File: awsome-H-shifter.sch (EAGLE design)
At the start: 8 parts

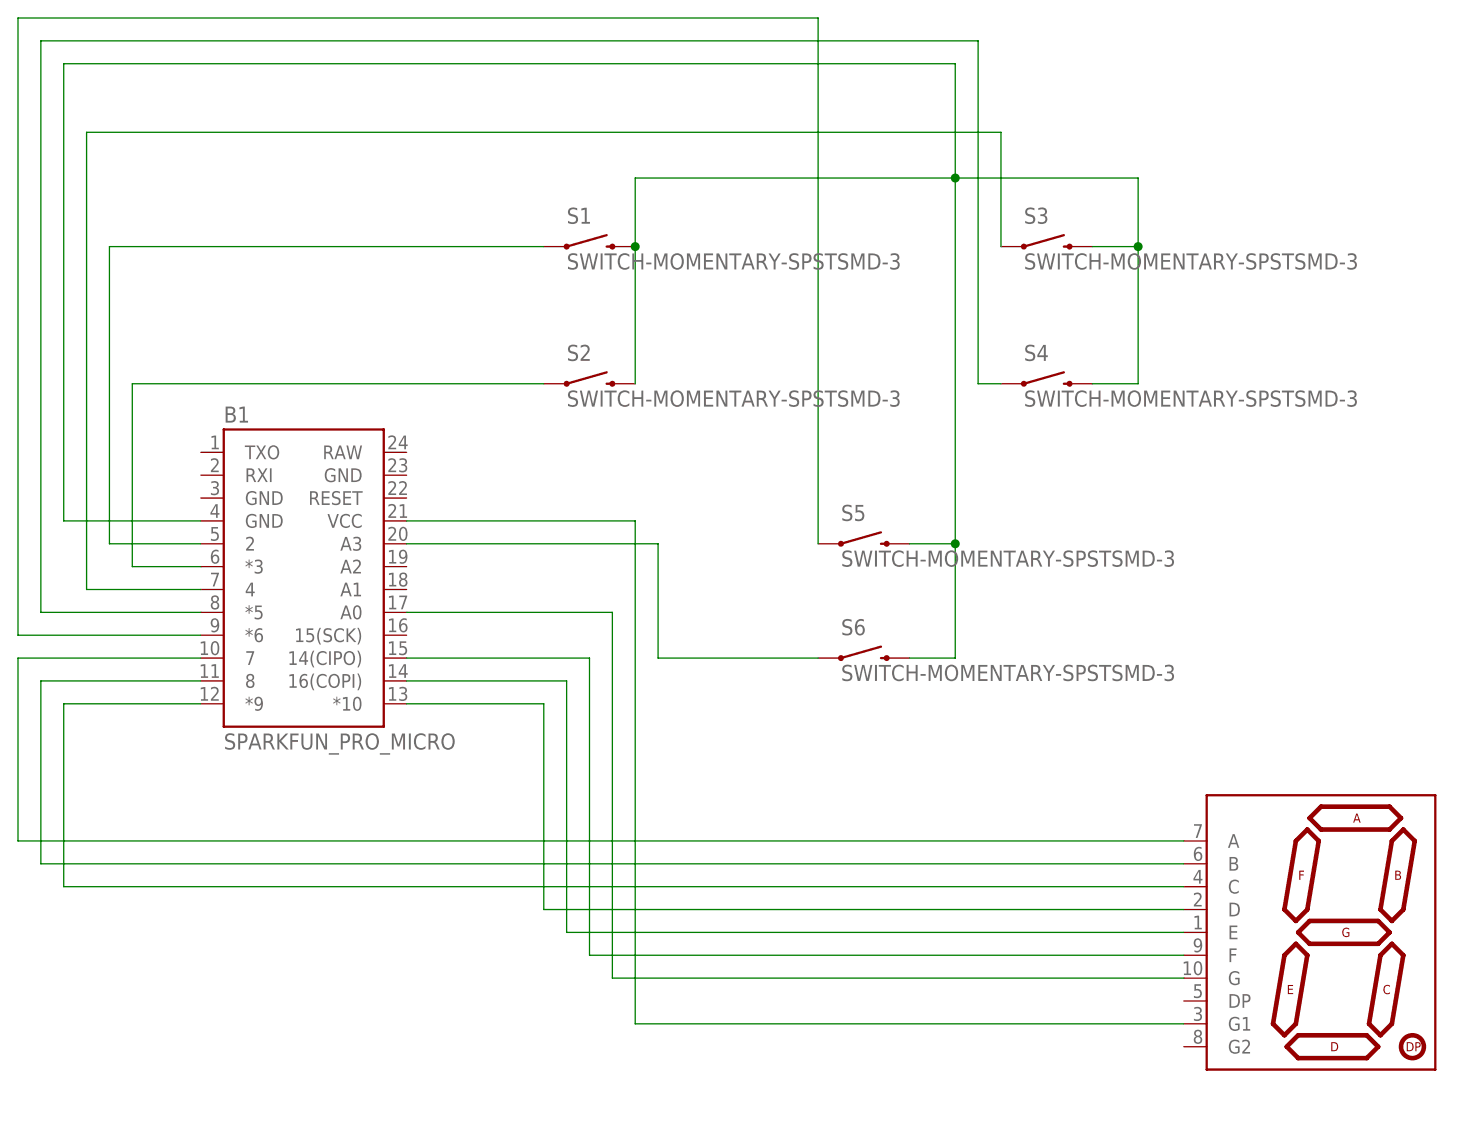
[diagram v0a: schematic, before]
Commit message: Add resistor library and R1 part to schematic
Integrated the 'Resistor' library with multiple resistor packages and symbols, and added a new resistor part R1 (300 Ω, 0402 package) to the schematic.
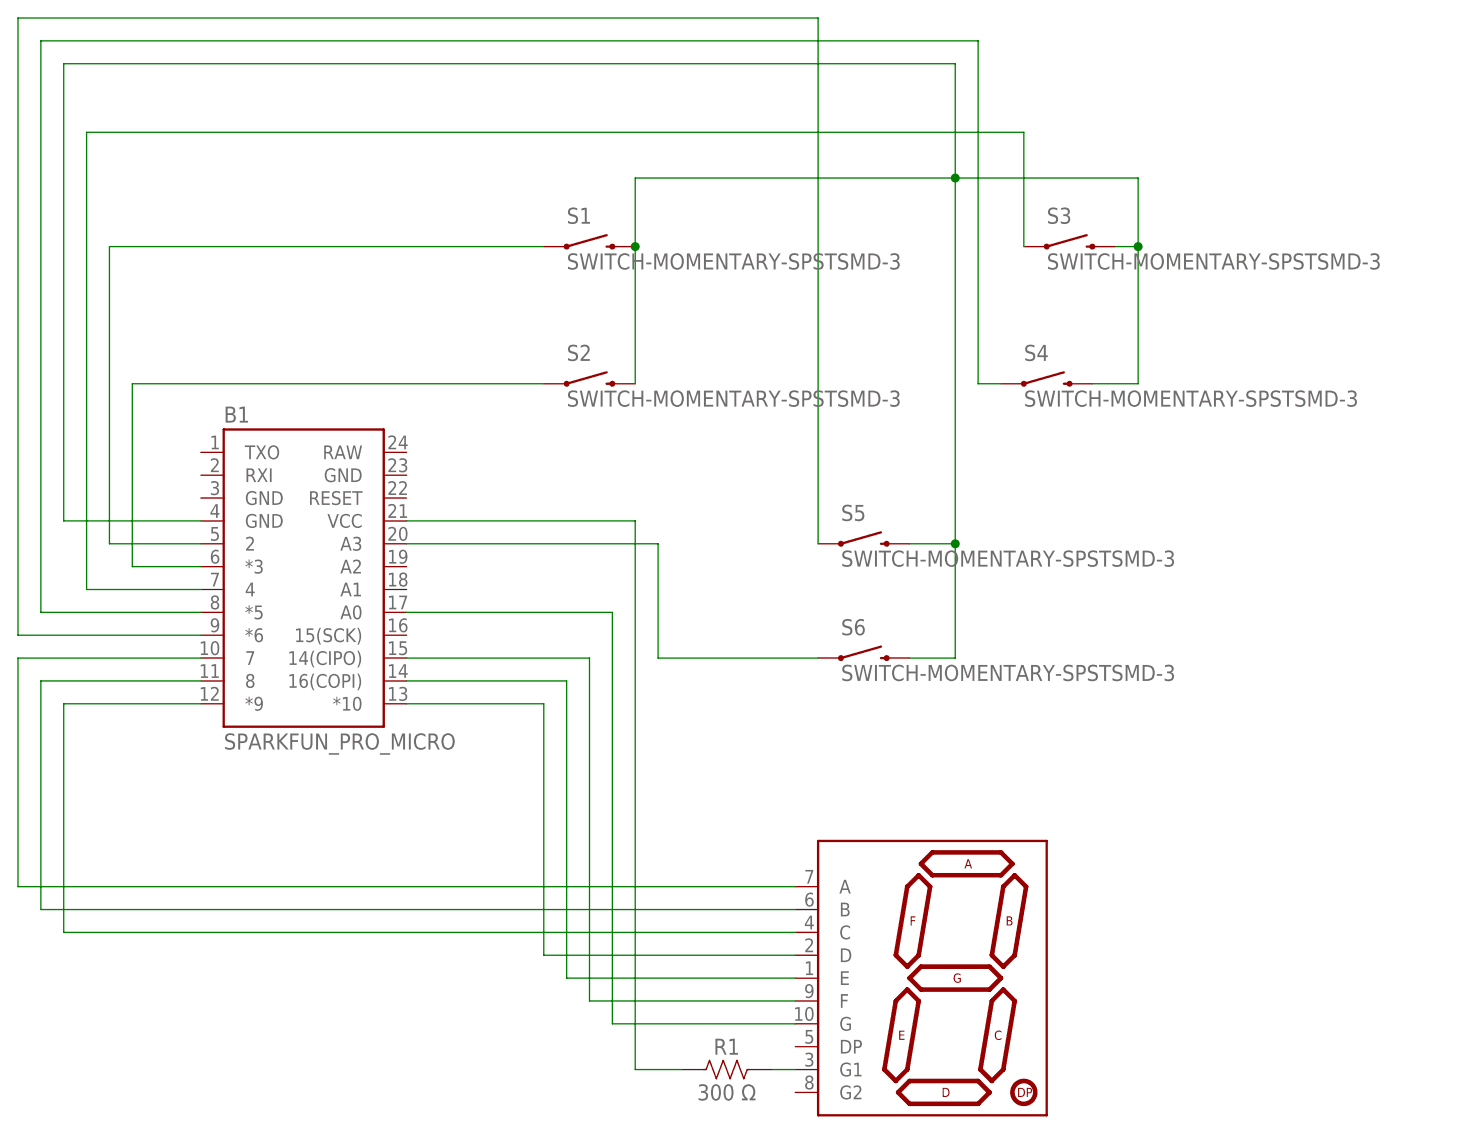
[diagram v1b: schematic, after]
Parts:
- added R1: 300 Ω, Resistor:R-US_CHIP-0402(1005-METRIC)
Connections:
- new net N$16: R1.2, U$1.G1
- net N$14: now also R1.1; no longer U$1.G1
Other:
- moved on the sheet: S3
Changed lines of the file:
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@@
 <part name="S5" library="SparkFun-Retired" library_urn="urn:adsk.eagle:library:533" deviceset="SWITCH-MOMENTARY-SPST" device="SMD-3" package3d_urn="urn:adsk.eagle:package:41386150/1"/>
 <part name="S6" library="SparkFun-Retired" library_urn="urn:adsk.eagle:library:533" deviceset="SWITCH-MOMENTARY-SPST" device="SMD-3" package3d_urn="urn:adsk.eagle:package:41386150/1"/>
+<part name="R1" library="Resistor" library_urn="urn:adsk.eagle:library:16378527" deviceset="R-US" device="CHIP-0402(1005-METRIC)" package3d_urn="urn:adsk.eagle:package:16378568/7" technology="_" value="300 Ω"/>
 </parts>
 <sheets>
@@
 <attribute name="VALUE" x="43.18" y="22.86" size="1.778" layer="96"/>
 </instance>
-<instance part="U$1" gate="G$1" x="167.64" y="2.54" smashed="yes"/>
+<instance part="U$1" gate="G$1" x="124.46" y="-2.54" smashed="yes"/>
 <instance part="S1" gate="G$1" x="83.82" y="78.74" smashed="yes">
 <attribute name="NAME" x="81.28" y="81.28" size="1.778" layer="95"/>
@@
 <attribute name="VALUE" x="81.28" y="60.96" size="1.778" layer="96"/>
 </instance>
-<instance part="S3" gate="G$1" x="134.62" y="78.74" smashed="yes">
-<attribute name="NAME" x="132.08" y="81.28" size="1.778" layer="95"/>
-<attribute name="VALUE" x="132.08" y="76.2" size="1.778" layer="96"/>
+<instance part="S3" gate="G$1" x="137.16" y="78.74" smashed="yes">
+<attribute name="NAME" x="134.62" y="81.28" size="1.778" layer="95"/>
+<attribute name="VALUE" x="134.62" y="76.2" size="1.778" layer="96"/>
 </instance>
 <instance part="S4" gate="G$1" x="134.62" y="63.5" smashed="yes">
@@
 <attribute name="NAME" x="111.76" y="35.56" size="1.778" layer="95"/>
 <attribute name="VALUE" x="111.76" y="30.48" size="1.778" layer="96"/>
+</instance>
+<instance part="R1" gate="G$1" x="99.06" y="-12.7" smashed="yes">
+<attribute name="NAME" x="99.06" y="-10.16" size="1.778" layer="95" align="center"/>
+<attribute name="VALUE" x="99.06" y="-15.24" size="1.778" layer="96" align="center"/>
 </instance>
 </instances>
@@
 <pinref part="S1" gate="G$1" pin="2"/>
 <wire x1="124.46" y1="86.36" x2="144.78" y2="86.36" width="0.1524" layer="91"/>
-<junction x="124.46" y="86.36"/>
 <wire x1="144.78" y1="86.36" x2="144.78" y2="78.74" width="0.1524" layer="91"/>
-<wire x1="144.78" y1="78.74" x2="139.7" y2="78.74" width="0.1524" layer="91"/>
+<wire x1="144.78" y1="78.74" x2="142.24" y2="78.74" width="0.1524" layer="91"/>
 <pinref part="S3" gate="G$1" pin="2"/>
 <wire x1="144.78" y1="78.74" x2="144.78" y2="63.5" width="0.1524" layer="91"/>
-<junction x="144.78" y="78.74"/>
 <wire x1="144.78" y1="63.5" x2="139.7" y2="63.5" width="0.1524" layer="91"/>
 <pinref part="S4" gate="G$1" pin="2"/>
 <wire x1="88.9" y1="78.74" x2="88.9" y2="63.5" width="0.1524" layer="91"/>
-<junction x="88.9" y="78.74"/>
 <pinref part="S2" gate="G$1" pin="2"/>
 <wire x1="124.46" y1="86.36" x2="124.46" y2="45.72" width="0.1524" layer="91"/>
@@
 <wire x1="124.46" y1="45.72" x2="124.46" y2="33.02" width="0.1524" layer="91"/>
 <wire x1="124.46" y1="33.02" x2="119.38" y2="33.02" width="0.1524" layer="91"/>
+<pinref part="S6" gate="G$1" pin="2"/>
+<junction x="124.46" y="86.36"/>
+<junction x="88.9" y="78.74"/>
+<junction x="144.78" y="78.74"/>
 <junction x="124.46" y="45.72"/>
-<pinref part="S6" gate="G$1" pin="2"/>
 </segment>
 </net>
@@
 <wire x1="40.64" y1="40.64" x2="27.94" y2="40.64" width="0.1524" layer="91"/>
 <wire x1="27.94" y1="40.64" x2="27.94" y2="91.44" width="0.1524" layer="91"/>
-<wire x1="27.94" y1="91.44" x2="129.54" y2="91.44" width="0.1524" layer="91"/>
-<wire x1="129.54" y1="91.44" x2="129.54" y2="78.74" width="0.1524" layer="91"/>
+<wire x1="27.94" y1="91.44" x2="132.08" y2="91.44" width="0.1524" layer="91"/>
+<wire x1="132.08" y1="91.44" x2="132.08" y2="78.74" width="0.1524" layer="91"/>
 <pinref part="S3" gate="G$1" pin="1"/>
 </segment>
@@
 <pinref part="B1" gate="G$1" pin="7"/>
 <wire x1="40.64" y1="33.02" x2="20.32" y2="33.02" width="0.1524" layer="91"/>
-<wire x1="20.32" y1="33.02" x2="20.32" y2="12.7" width="0.1524" layer="91"/>
-<wire x1="20.32" y1="12.7" x2="149.86" y2="12.7" width="0.1524" layer="91"/>
+<wire x1="20.32" y1="33.02" x2="20.32" y2="7.62" width="0.1524" layer="91"/>
+<wire x1="20.32" y1="7.62" x2="106.68" y2="7.62" width="0.1524" layer="91"/>
 <pinref part="U$1" gate="G$1" pin="A"/>
 </segment>
@@
 <pinref part="B1" gate="G$1" pin="8"/>
 <wire x1="40.64" y1="30.48" x2="22.86" y2="30.48" width="0.1524" layer="91"/>
-<wire x1="22.86" y1="30.48" x2="22.86" y2="10.16" width="0.1524" layer="91"/>
-<wire x1="22.86" y1="10.16" x2="149.86" y2="10.16" width="0.1524" layer="91"/>
+<wire x1="22.86" y1="30.48" x2="22.86" y2="5.08" width="0.1524" layer="91"/>
+<wire x1="22.86" y1="5.08" x2="106.68" y2="5.08" width="0.1524" layer="91"/>
 <pinref part="U$1" gate="G$1" pin="B"/>
 </segment>
@@
 <pinref part="B1" gate="G$1" pin="*9"/>
 <wire x1="40.64" y1="27.94" x2="25.4" y2="27.94" width="0.1524" layer="91"/>
-<wire x1="25.4" y1="27.94" x2="25.4" y2="7.62" width="0.1524" layer="91"/>
-<wire x1="25.4" y1="7.62" x2="149.86" y2="7.62" width="0.1524" layer="91"/>
+<wire x1="25.4" y1="27.94" x2="25.4" y2="2.54" width="0.1524" layer="91"/>
+<wire x1="25.4" y1="2.54" x2="106.68" y2="2.54" width="0.1524" layer="91"/>
 <pinref part="U$1" gate="G$1" pin="C"/>
 </segment>
@@
 <pinref part="B1" gate="G$1" pin="*10"/>
 <wire x1="63.5" y1="27.94" x2="78.74" y2="27.94" width="0.1524" layer="91"/>
-<wire x1="78.74" y1="27.94" x2="78.74" y2="5.08" width="0.1524" layer="91"/>
-<wire x1="78.74" y1="5.08" x2="149.86" y2="5.08" width="0.1524" layer="91"/>
+<wire x1="78.74" y1="27.94" x2="78.74" y2="0" width="0.1524" layer="91"/>
+<wire x1="78.74" y1="0" x2="106.68" y2="0" width="0.1524" layer="91"/>
 <pinref part="U$1" gate="G$1" pin="D"/>
 </segment>
@@
 <pinref part="B1" gate="G$1" pin="16(COPI)"/>
 <wire x1="63.5" y1="30.48" x2="81.28" y2="30.48" width="0.1524" layer="91"/>
-<wire x1="81.28" y1="30.48" x2="81.28" y2="2.54" width="0.1524" layer="91"/>
-<wire x1="81.28" y1="2.54" x2="149.86" y2="2.54" width="0.1524" layer="91"/>
+<wire x1="81.28" y1="30.48" x2="81.28" y2="-2.54" width="0.1524" layer="91"/>
+<wire x1="81.28" y1="-2.54" x2="106.68" y2="-2.54" width="0.1524" layer="91"/>
 <pinref part="U$1" gate="G$1" pin="E"/>
 </segment>
@@
 <pinref part="B1" gate="G$1" pin="14(CIPO)"/>
 <wire x1="63.5" y1="33.02" x2="83.82" y2="33.02" width="0.1524" layer="91"/>
-<wire x1="83.82" y1="33.02" x2="83.82" y2="0" width="0.1524" layer="91"/>
-<wire x1="83.82" y1="0" x2="149.86" y2="0" width="0.1524" layer="91"/>
+<wire x1="83.82" y1="33.02" x2="83.82" y2="-5.08" width="0.1524" layer="91"/>
+<wire x1="83.82" y1="-5.08" x2="106.68" y2="-5.08" width="0.1524" layer="91"/>
 <pinref part="U$1" gate="G$1" pin="F"/>
 </segment>
@@
 <pinref part="B1" gate="G$1" pin="A0"/>
 <wire x1="63.5" y1="38.1" x2="86.36" y2="38.1" width="0.1524" layer="91"/>
-<wire x1="86.36" y1="38.1" x2="86.36" y2="-2.54" width="0.1524" layer="91"/>
-<wire x1="86.36" y1="-2.54" x2="149.86" y2="-2.54" width="0.1524" layer="91"/>
+<wire x1="86.36" y1="38.1" x2="86.36" y2="-7.62" width="0.1524" layer="91"/>
+<wire x1="86.36" y1="-7.62" x2="106.68" y2="-7.62" width="0.1524" layer="91"/>
 <pinref part="U$1" gate="G$1" pin="G"/>
 </segment>
@@
 <pinref part="B1" gate="G$1" pin="VCC"/>
 <wire x1="63.5" y1="48.26" x2="88.9" y2="48.26" width="0.1524" layer="91"/>
-<wire x1="88.9" y1="48.26" x2="88.9" y2="-7.62" width="0.1524" layer="91"/>
-<wire x1="88.9" y1="-7.62" x2="149.86" y2="-7.62" width="0.1524" layer="91"/>
-<pinref part="U$1" gate="G$1" pin="G1"/>
+<wire x1="88.9" y1="48.26" x2="88.9" y2="-12.7" width="0.1524" layer="91"/>
+<wire x1="88.9" y1="-12.7" x2="93.98" y2="-12.7" width="0.1524" layer="91"/>
+<pinref part="R1" gate="G$1" pin="1"/>
 </segment>
 </net>
@@
 </segment>
 </net>
+<net name="N$16" class="0">
+<segment>
+<pinref part="U$1" gate="G$1" pin="G1"/>
+<wire x1="104.14" y1="-12.7" x2="106.68" y2="-12.7" width="0.1524" layer="91"/>
+<pinref part="R1" gate="G$1" pin="2"/>
+</segment>
+</net>
 </nets>
 </sheet>
@@
 <sch_hier_ref_des_map>
 <part_path_ref_des_mapping board_ref_des="B1" logical_identifier="B1"/>
+<part_path_ref_des_mapping board_ref_des="R1" logical_identifier="R1"/>
 <part_path_ref_des_mapping board_ref_des="S1" logical_identifier="S1"/>
 <part_path_ref_des_mapping board_ref_des="S2" logical_identifier="S2"/>
@@
 packages will not be understood (or retained) with this version.
 </note>
+<note version="8.4" severity="warning">
+Since Version 8.4, EAGLE supports properties for SPICE simulation.
+Probes in schematics and SPICE mapping objects found in parts and library devices
+will not be understood with this version. Update EAGLE to the latest version
+for full support of SPICE simulation.
+</note>
 </compatibility>
